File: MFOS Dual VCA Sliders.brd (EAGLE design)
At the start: 97.5 x 50.8 mm, 61 parts, among them IC1 TL072P, IC2 LM13700N, Q1 2N3904, Q2 2N3904, Q3 2N3906, Q4 2N3906, U1 POWER

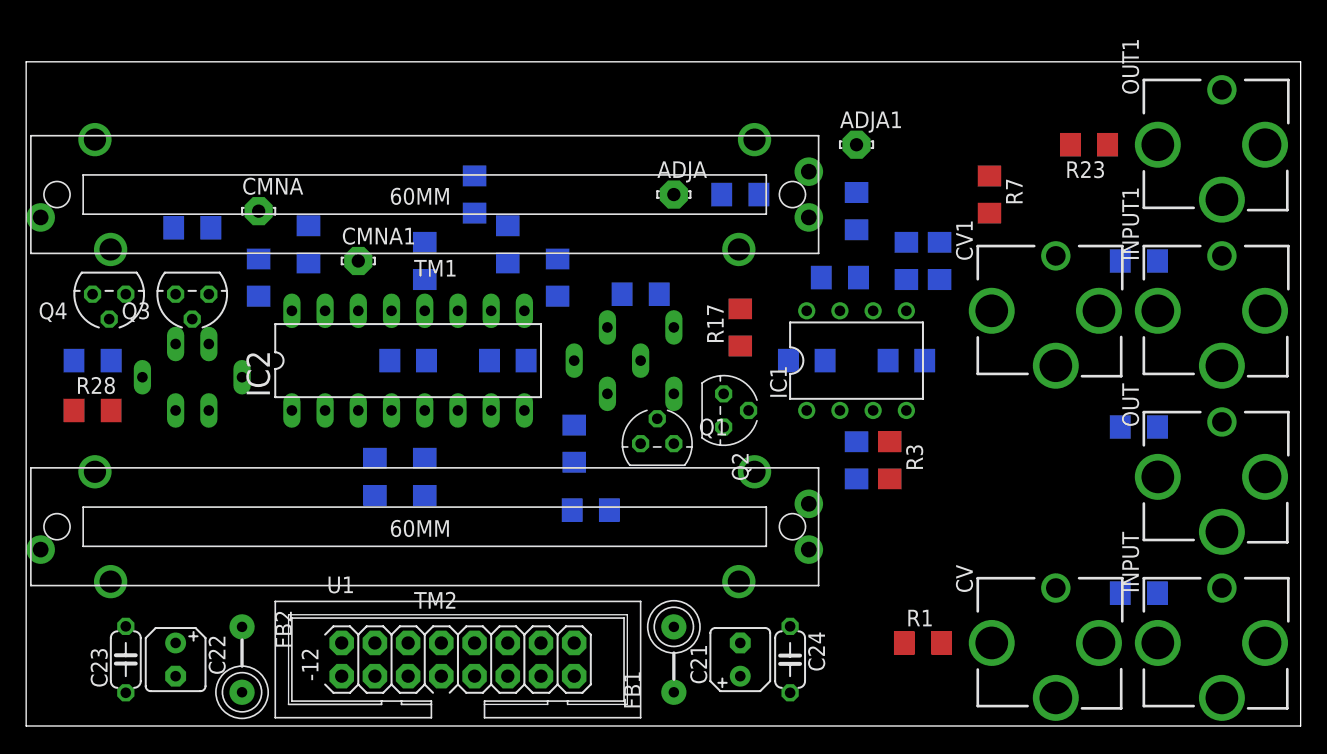
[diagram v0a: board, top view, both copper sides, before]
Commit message: routed with smt resistors
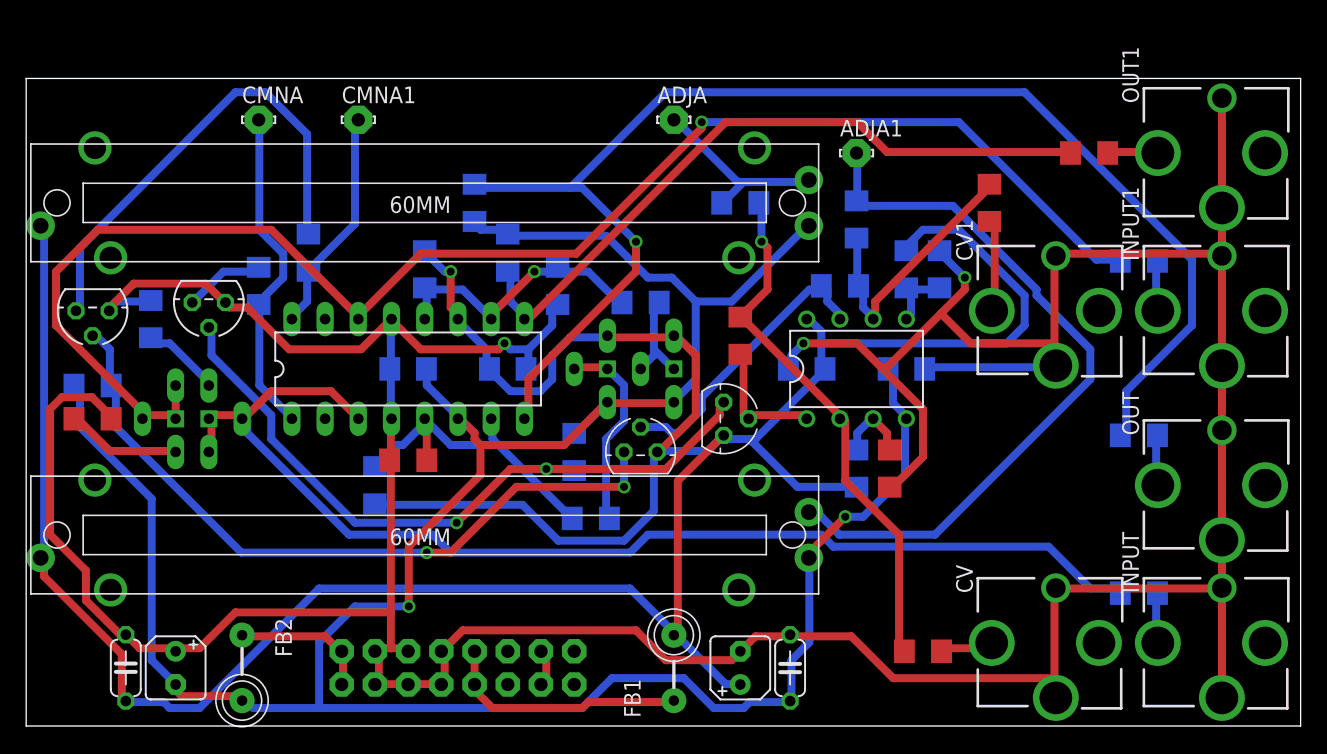
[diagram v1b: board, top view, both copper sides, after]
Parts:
- moved CMNA1 10.8 mm to (25.4, 46.4)
- moved R20 7.67 mm to (9.53, 31.1), turned to 90 degrees
- moved CMNA 6.98 mm to (17.8, 46.4)
- moved ADJA 5.71 mm to (49.5, 46.4)
- moved TRIM_A 3.18 mm to (14.0, 23.5)
- moved TRIM_A1 3.18 mm to (11.4, 23.5)
- moved R11 1.91 mm to (5.08, 26.0)
- moved Q4 1.80 mm to (5.08, 31.8)
- moved R18 1.80 mm to (29.2, 20.3), flipped to the top, turned to 180 degrees
- moved Q3 1.42 mm to (14.0, 32.4)
- moved Q1 1.42 mm to (47.0, 21.0)
- moved ADJA1 0.64 mm to (63.5, 43.8)
- moved OUT1 0.64 mm to (91.4, 43.8)
- moved R23 0.64 mm to (81.3, 43.8)
- moved R25 0.64 mm to (30.5, 34.9)
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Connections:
- net N$18: now also BIAS.P$1
- net N$23: now also TRIM_A.P$1
- net N$28: now also BIAS1.P$1
- net N$30: now also TRIM_A1.P$1
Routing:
- net GND: track 0.00 -> 328.8 mm, vias 0 -> 3
- net +12V: track 0.00 -> 238.8 mm, vias 0 -> 1
- net -12V: track 0.00 -> 200.6 mm, vias 0 -> 2
- net N$30: track 0.00 -> 115.8 mm, vias 0 -> 1
- net N$20: track 0.00 -> 103.1 mm, vias 0 -> 1
- net N$23: track 0.00 -> 90.8 mm
- net N$9: track 0.00 -> 56.3 mm
- net N$14: track 0.00 -> 55.5 mm, vias 0 -> 2
- net N$7: track 0.00 -> 54.2 mm, vias 0 -> 2
- net N$25: track 0.00 -> 53.2 mm
- net N$6: track 0.00 -> 40.8 mm, vias 0 -> 1
- net N$15: track 0.00 -> 36.3 mm
- net N$16: track 0.00 -> 25.4 mm
- net N$21: track 0.00 -> 25.3 mm
- net N$1: track 0.00 -> 22.5 mm
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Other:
- board size 97.5 x 50.8 mm -> 97.5 x 49.5 mm
